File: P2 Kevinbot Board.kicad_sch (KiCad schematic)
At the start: 16 parts, among them J1 Conn_01x03_Pin, J12 Conn_02x06_Odd_Even, J16 Conn_02x06_Odd_Even, J2 Conn_01x03_Pin, J6 Conn_02x06_Odd_Even, J8 Conn_02x06_Odd_Even, J9 Conn_01x02_Pin, SW1 SW_Push, U1 P2_EDGE_MODULE_SOCKET

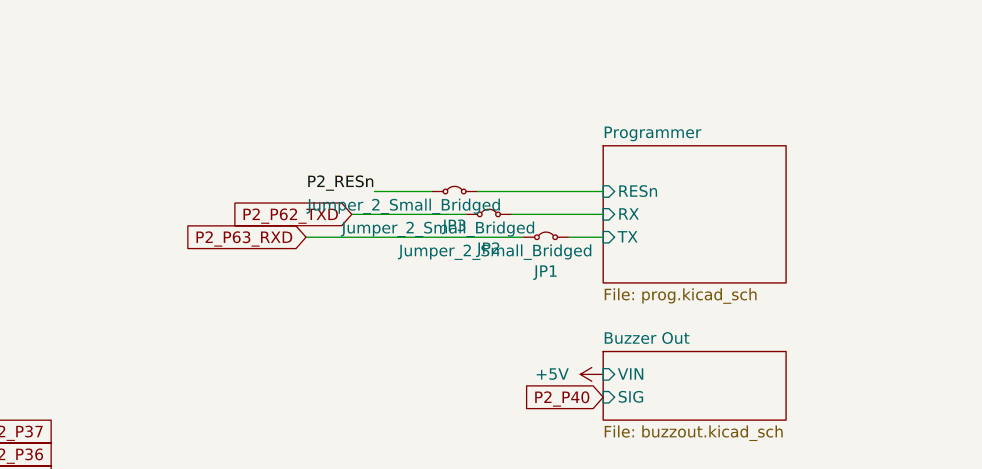
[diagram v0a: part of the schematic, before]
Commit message: prog, pgmmux, sch: hierarchical organization, prep for programmer mux
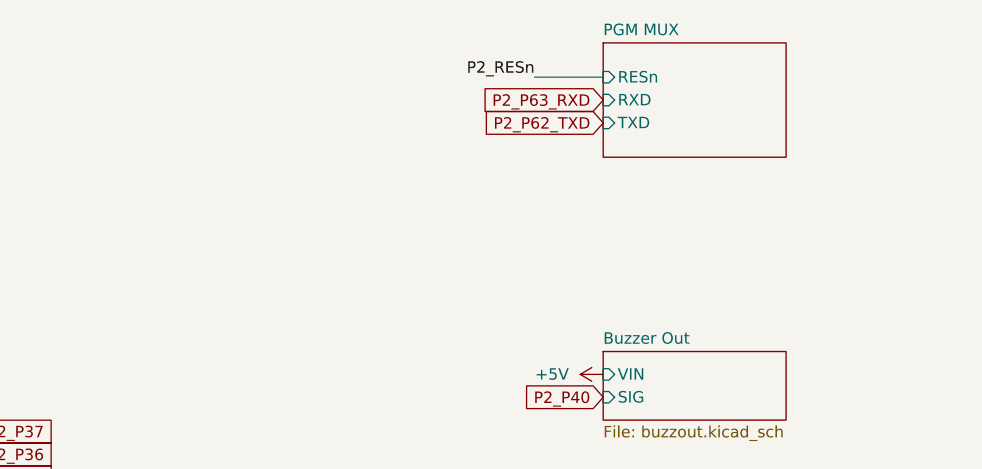
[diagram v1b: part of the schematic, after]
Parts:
- removed JP1, JP2, JP3: Jumper_2_Small_Bridged, Jumper:SolderJumper-2_P1.3mm_Bridged_RoundedPad1.0x1.5mm, symbol Jumper:Jumper_2_Small_Bridged
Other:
- removed sheet Programmer
- added sheet PGM MUX (pgmmux.kicad_sch)

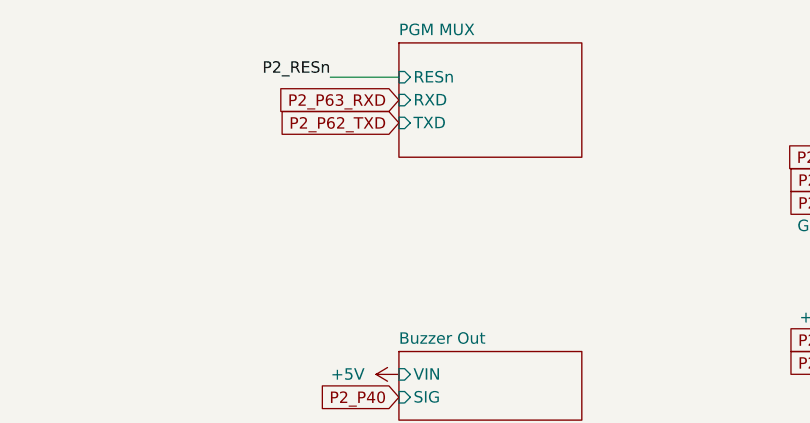
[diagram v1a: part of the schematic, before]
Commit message: pgmmux, pcb: add selector switch
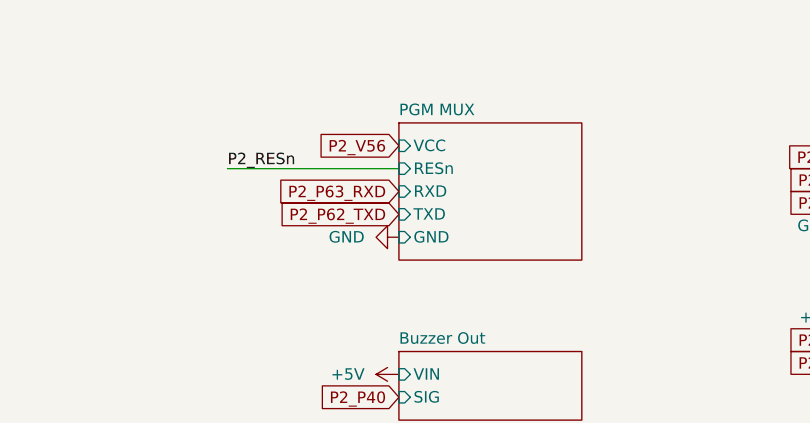
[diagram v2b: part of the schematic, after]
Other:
- sheet PGM MUX ports: added GND, VCC; removed none
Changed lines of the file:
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@@
 	(wire
 		(pts
-			(xy 148.59 20.32) (xy 156.21 20.32)
+			(xy 137.16 30.48) (xy 156.21 30.48)
 		)
 		(stroke
@@
 	)
 	(label "P2_RESn"
-		(at 148.59 20.32 180)
+		(at 137.16 30.48 0)
 		(effects
 			(font
 				(size 1.27 1.27)
 			)
-			(justify right bottom)
+			(justify left bottom)
 		)
 	)
@@
 	(global_label "P2_P63_RXD"
 		(shape input)
-		(at 156.21 22.86 180)
+		(at 156.21 33.02 180)
 		(fields_autoplaced yes)
 		(effects
@@
 		)
 		(property "Intersheetrefs" "${INTERSHEET_REFS}"
-			(at 141.9436 22.9394 0)
+			(at 141.9436 33.0994 0)
 			(effects
 				(font
@@
 		)
 	)
+	(global_label "P2_V56"
+		(shape input)
+		(at 156.21 27.94 180)
+		(fields_autoplaced yes)
+		(effects
+			(font
+				(size 1.27 1.27)
+			)
+			(justify right)
+		)
+		(property "Intersheetrefs" "${INTERSHEET_REFS}"
+			(at 146.2701 27.94 0)
+			(effects
+				(font
+					(size 1.27 1.27)
+				)
+				(justify right)
+				(hide yes)
+			)
+		)
+	)
 	(global_label "P2_P11"
 		(shape input)
@@
 	(global_label "P2_P62_TXD"
 		(shape input)
-		(at 156.21 25.4 180)
+		(at 156.21 35.56 180)
 		(fields_autoplaced yes)
 		(effects
@@
 		)
 		(property "Intersheetrefs" "${INTERSHEET_REFS}"
-			(at 142.2459 25.4794 0)
+			(at 142.2459 35.6394 0)
 			(effects
 				(font
@@
 		)
 	)
+	(symbol
+		(lib_id "power:GND")
+		(at 156.21 38.1 270)
+		(unit 1)
+		(exclude_from_sim no)
+		(in_bom yes)
+		(on_board yes)
+		(dnp no)
+		(fields_autoplaced yes)
+		(property "Reference" "#PWR051"
+			(at 149.86 38.1 0)
+			(effects
+				(font
+					(size 1.27 1.27)
+				)
+				(hide yes)
+			)
+		)
+		(property "Value" "GND"
+			(at 152.4 38.0999 90)
+			(effects
+				(font
+					(size 1.27 1.27)
+				)
+				(justify right)
+			)
+		)
+		(property "Footprint" ""
+			(at 156.21 38.1 0)
+			(effects
+				(font
+					(size 1.27 1.27)
+				)
+				(hide yes)
+			)
+		)
+		(property "Datasheet" ""
+			(at 156.21 38.1 0)
+			(effects
+				(font
+					(size 1.27 1.27)
+				)
+				(hide yes)
+			)
+		)
+		(property "Description" "Power symbol creates a global label with name \"GND\" , ground"
+			(at 156.21 38.1 0)
+			(effects
+				(font
+					(size 1.27 1.27)
+				)
+				(hide yes)
+			)
+		)
+		(pin "1"
+		)
+		(instances
+			(project "P2 Kevinbot Board"
+				(path "/362ca48c-0b77-4943-b8b3-fc15ab97f30d"
+					(reference "#PWR051")
+					(unit 1)
+				)
+			)
+		)
+	)
 	(sheet
 		(at 208.28 95.25)
@@
 	)
 	(sheet
-		(at 156.21 16.51)
-		(size 20.32 12.7)
+		(at 156.21 25.4)
+		(size 20.32 15.24)
 		(exclude_from_sim no)
 		(in_bom yes)
@@
 		)
 		(property "Sheetname" "PGM MUX"
-			(at 156.21 15.7984 0)
+			(at 156.21 24.6884 0)
 			(effects
 				(font
@@
 		)
 		(property "Sheetfile" "pgmmux.kicad_sch"
-			(at 156.21 29.7946 0)
+			(at 156.21 41.2246 0)
 			(effects
 				(font
@@
 		)
 		(pin "RESn" input
-			(at 156.21 20.32 180)
+			(at 156.21 30.48 180)
 			(effects
 				(font
@@
 		)
 		(pin "RXD" input
-			(at 156.21 22.86 180)
+			(at 156.21 33.02 180)
 			(effects
 				(font
@@
 		)
 		(pin "TXD" input
-			(at 156.21 25.4 180)
+			(at 156.21 35.56 180)
+			(effects
+				(font
+					(size 1.27 1.27)
+				)
+				(justify left)
+			)
+		)
+		(pin "GND" input
+			(at 156.21 38.1 180)
+			(effects
+				(font
+					(size 1.27 1.27)
+				)
+				(justify left)
+			)
+		)
+		(pin "VCC" input
+			(at 156.21 27.94 180)
 			(effects
 				(font

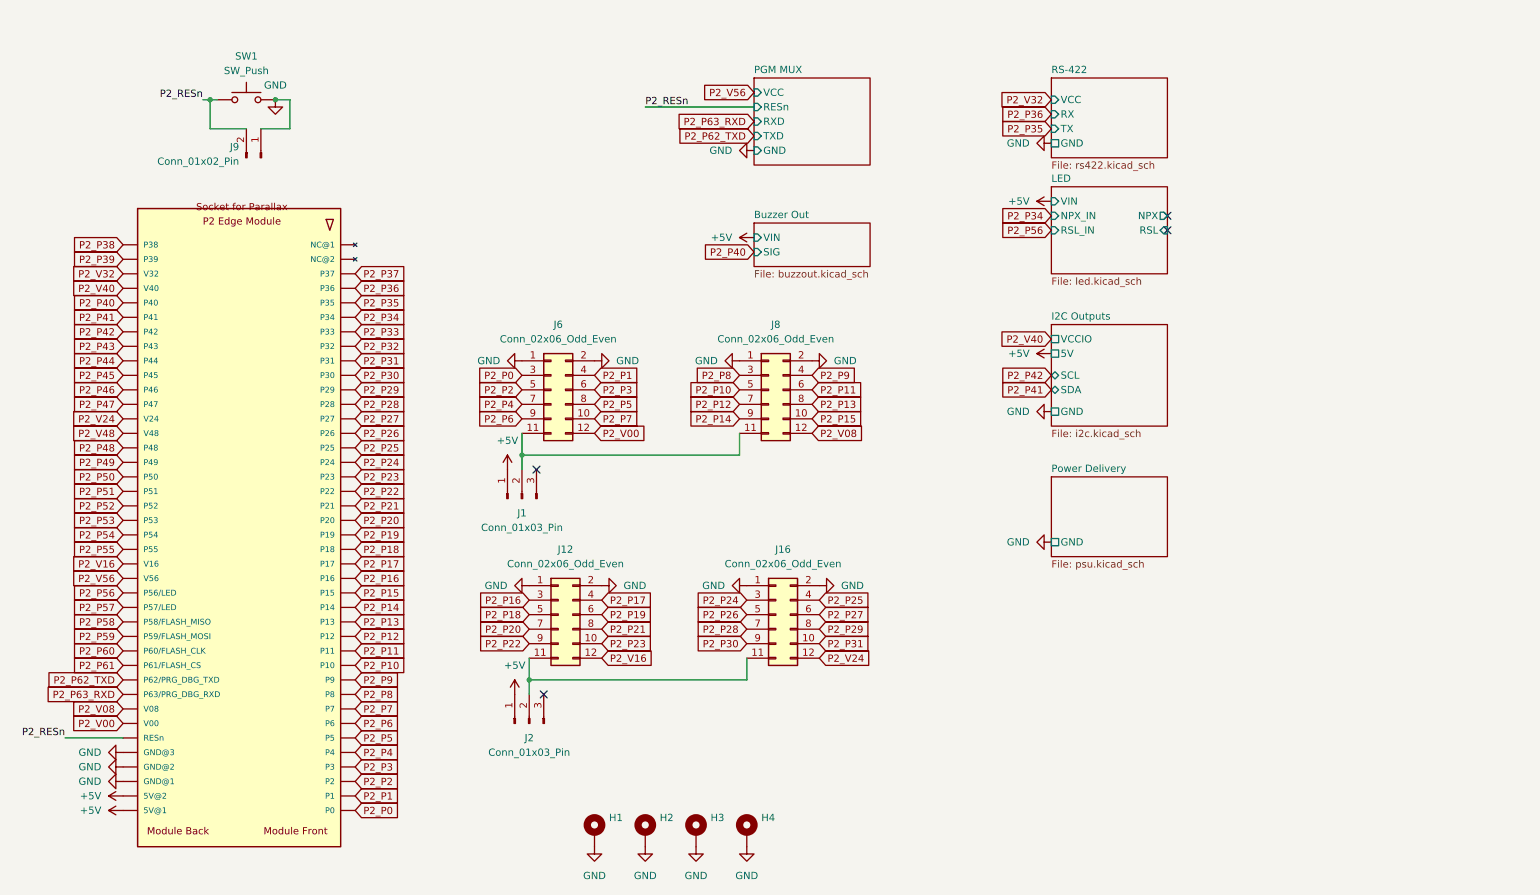
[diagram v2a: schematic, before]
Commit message: pgmmux, pcb:  ext connectors
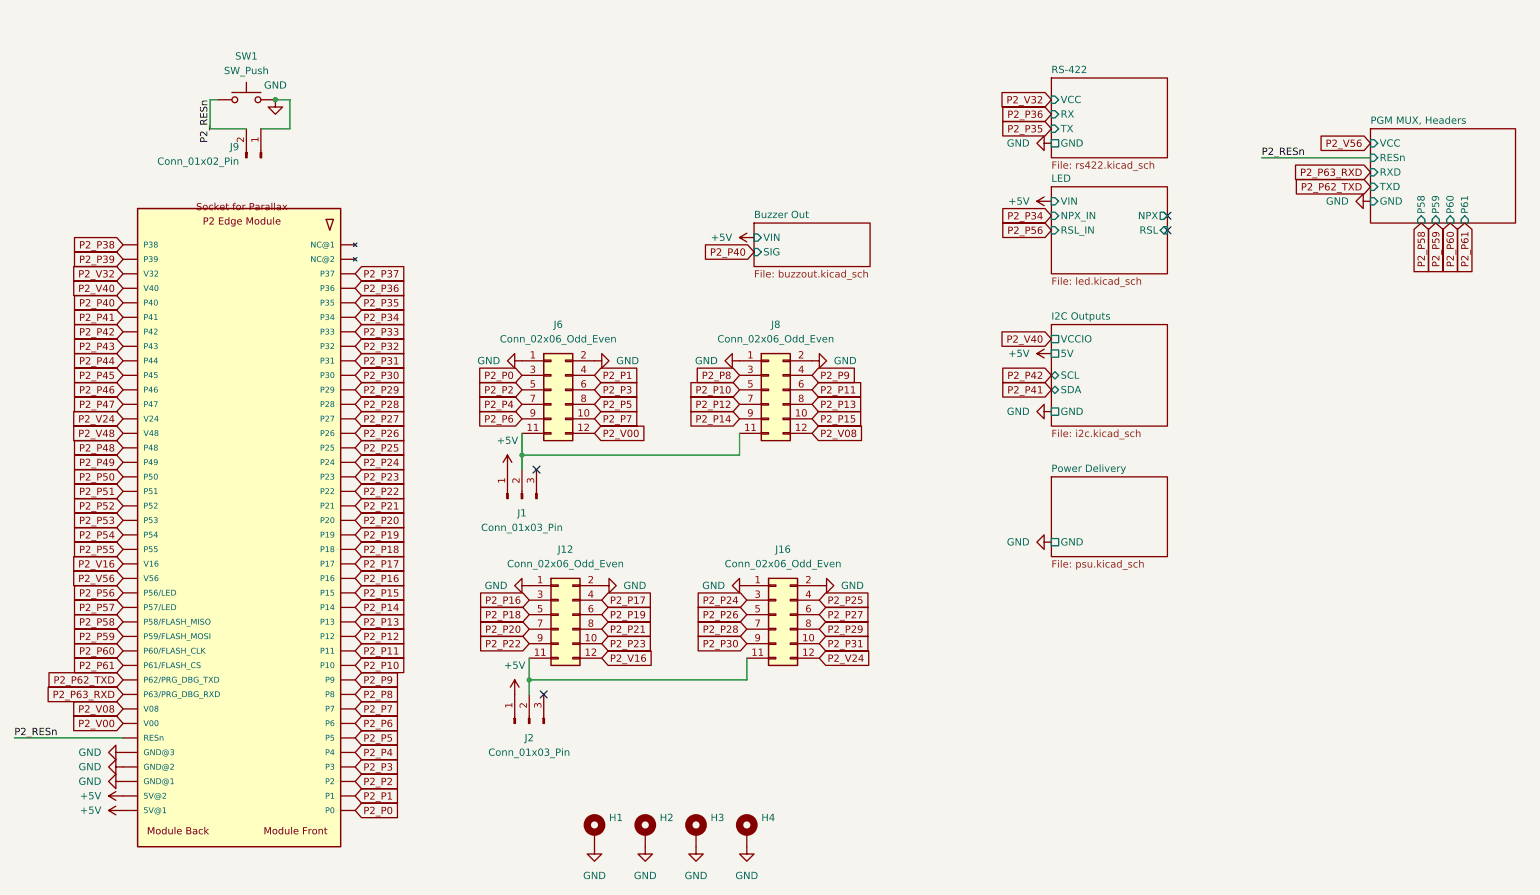
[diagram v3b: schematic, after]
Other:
- sheet PGM MUX renamed PGM MUX, Headers
- sheet PGM MUX, Headers ports: added P58, P59, P60, P61; removed none
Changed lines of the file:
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@@
 	)
 	(junction
-		(at 60.96 29.21)
-		(diameter 0)
-		(color 0 0 0 0)
-	)
-	(junction
 		(at 72.39 29.21)
 		(diameter 0)
@@
 	(wire
 		(pts
-			(xy 35.56 140.97) (xy 45.72 140.97)
+			(xy 26.67 140.97) (xy 45.72 140.97)
 		)
 		(stroke
@@
 	(wire
 		(pts
-			(xy 59.69 29.21) (xy 60.96 29.21)
-		)
-		(stroke
-			(width 0)
-			(type default)
-		)
-	)
-	(wire
-		(pts
 			(xy 115.57 91.44) (xy 115.57 93.98)
 		)
@@
 	(wire
 		(pts
-			(xy 137.16 30.48) (xy 156.21 30.48)
+			(xy 245.11 39.37) (xy 264.16 39.37)
 		)
 		(stroke
@@
 	)
 	(label "P2_RESn"
-		(at 137.16 30.48 0)
+		(at 245.11 39.37 0)
 		(effects
 			(font
@@
 	)
 	(label "P2_RESn"
-		(at 59.69 29.21 180)
+		(at 60.96 29.21 270)
 		(effects
 			(font
@@
 	)
 	(label "P2_RESn"
-		(at 35.56 140.97 180)
+		(at 26.67 140.97 0)
 		(effects
 			(font
 				(size 1.27 1.27)
 			)
-			(justify right bottom)
+			(justify left bottom)
 		)
 	)
@@
 	(global_label "P2_P63_RXD"
 		(shape input)
-		(at 156.21 33.02 180)
+		(at 264.16 41.91 180)
 		(fields_autoplaced yes)
 		(effects
@@
 		)
 		(property "Intersheetrefs" "${INTERSHEET_REFS}"
-			(at 141.9436 33.0994 0)
+			(at 249.8936 41.9894 0)
 			(effects
 				(font
@@
 	(global_label "P2_V56"
 		(shape input)
-		(at 156.21 27.94 180)
+		(at 264.16 36.83 180)
 		(fields_autoplaced yes)
 		(effects
@@
 		)
 		(property "Intersheetrefs" "${INTERSHEET_REFS}"
-			(at 146.2701 27.94 0)
+			(at 254.2201 36.83 0)
 			(effects
 				(font
@@
 		)
 	)
+	(global_label "P2_P59"
+		(shape input)
+		(at 275.59 50.8 270)
+		(fields_autoplaced yes)
+		(effects
+			(font
+				(size 1.27 1.27)
+			)
+			(justify right)
+		)
+		(property "Intersheetrefs" "${INTERSHEET_REFS}"
+			(at 275.59 60.9213 90)
+			(effects
+				(font
+					(size 1.27 1.27)
+				)
+				(justify right)
+				(hide yes)
+			)
+		)
+	)
 	(global_label "P2_P43"
 		(shape input)
@@
 		)
 	)
+	(global_label "P2_P58"
+		(shape input)
+		(at 273.05 50.8 270)
+		(fields_autoplaced yes)
+		(effects
+			(font
+				(size 1.27 1.27)
+			)
+			(justify right)
+		)
+		(property "Intersheetrefs" "${INTERSHEET_REFS}"
+			(at 273.05 60.9213 90)
+			(effects
+				(font
+					(size 1.27 1.27)
+				)
+				(justify right)
+				(hide yes)
+			)
+		)
+	)
 	(global_label "P2_V56"
 		(shape input)
@@
 		)
 	)
+	(global_label "P2_P60"
+		(shape input)
+		(at 278.13 50.8 270)
+		(fields_autoplaced yes)
+		(effects
+			(font
+				(size 1.27 1.27)
+			)
+			(justify right)
+		)
+		(property "Intersheetrefs" "${INTERSHEET_REFS}"
+			(at 278.13 60.9213 90)
+			(effects
+				(font
+					(size 1.27 1.27)
+				)
+				(justify right)
+				(hide yes)
+			)
+		)
+	)
 	(global_label "P2_P33"
 		(shape input)
@@
 	(global_label "P2_P62_TXD"
 		(shape input)
-		(at 156.21 35.56 180)
+		(at 264.16 44.45 180)
 		(fields_autoplaced yes)
 		(effects
@@
 		)
 		(property "Intersheetrefs" "${INTERSHEET_REFS}"
-			(at 142.2459 35.6394 0)
+			(at 250.1959 44.5294 0)
 			(effects
 				(font
@@
 		)
 	)
+	(global_label "P2_P61"
+		(shape input)
+		(at 280.67 50.8 270)
+		(fields_autoplaced yes)
+		(effects
+			(font
+				(size 1.27 1.27)
+			)
+			(justify right)
+		)
+		(property "Intersheetrefs" "${INTERSHEET_REFS}"
+			(at 280.67 60.9213 90)
+			(effects
+				(font
+					(size 1.27 1.27)
+				)
+				(justify right)
+				(hide yes)
+			)
+		)
+	)
 	(global_label "P2_P12"
 		(shape input)
@@
 	(symbol
 		(lib_id "power:GND")
-		(at 156.21 38.1 270)
+		(at 264.16 46.99 270)
 		(unit 1)
 		(exclude_from_sim no)
@@
 		(fields_autoplaced yes)
 		(property "Reference" "#PWR051"
-			(at 149.86 38.1 0)
+			(at 257.81 46.99 0)
 			(effects
 				(font
@@
 		)
 		(property "Value" "GND"
-			(at 152.4 38.0999 90)
+			(at 260.35 46.9899 90)
 			(effects
 				(font
@@
 		)
 		(property "Footprint" ""
-			(at 156.21 38.1 0)
+			(at 264.16 46.99 0)
 			(effects
 				(font
@@
 		)
 		(property "Datasheet" ""
-			(at 156.21 38.1 0)
+			(at 264.16 46.99 0)
 			(effects
 				(font
@@
 		)
 		(property "Description" "Power symbol creates a global label with name \"GND\" , ground"
-			(at 156.21 38.1 0)
+			(at 264.16 46.99 0)
 			(effects
 				(font
@@
 	)
 	(sheet
-		(at 156.21 25.4)
-		(size 20.32 15.24)
+		(at 264.16 34.29)
+		(size 25.4 16.51)
 		(exclude_from_sim no)
 		(in_bom yes)
@@
 			(color 0 0 0 0.0000)
 		)
-		(property "Sheetname" "PGM MUX"
-			(at 156.21 24.6884 0)
+		(property "Sheetname" "PGM MUX, Headers"
+			(at 264.16 33.5784 0)
 			(effects
 				(font
@@
 		)
 		(property "Sheetfile" "pgmmux.kicad_sch"
-			(at 156.21 41.2246 0)
+			(at 264.16 51.3846 0)
 			(effects
 				(font
@@
 		)
 		(pin "RESn" input
-			(at 156.21 30.48 180)
+			(at 264.16 39.37 180)
 			(effects
 				(font
@@
 		)
 		(pin "RXD" input
-			(at 156.21 33.02 180)
+			(at 264.16 41.91 180)
 			(effects
 				(font
@@
 		)
 		(pin "TXD" input
-			(at 156.21 35.56 180)
+			(at 264.16 44.45 180)
 			(effects
 				(font
@@
 		)
 		(pin "GND" input
-			(at 156.21 38.1 180)
+			(at 264.16 46.99 180)
 			(effects
 				(font
@@
 		)
 		(pin "VCC" input
-			(at 156.21 27.94 180)
+			(at 264.16 36.83 180)
+			(effects
+				(font
+					(size 1.27 1.27)
+				)
+				(justify left)
+			)
+		)
+		(pin "P58" input
+			(at 273.05 50.8 270)
+			(effects
+				(font
+					(size 1.27 1.27)
+				)
+				(justify left)
+			)
+		)
+		(pin "P59" input
+			(at 275.59 50.8 270)
+			(effects
+				(font
+					(size 1.27 1.27)
+				)
+				(justify left)
+			)
+		)
+		(pin "P60" input
+			(at 278.13 50.8 270)
+			(effects
+				(font
+					(size 1.27 1.27)
+				)
+				(justify left)
+			)
+		)
+		(pin "P61" input
+			(at 280.67 50.8 270)
 			(effects
 				(font
